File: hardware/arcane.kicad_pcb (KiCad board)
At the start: 2 copper layers, 24.8 x 28.5 mm, 7 parts, among them J1 Conn_01x02, J2 Conn_01x07, SW1 SW_Push, U1 XIAO-nRF52840-SMD

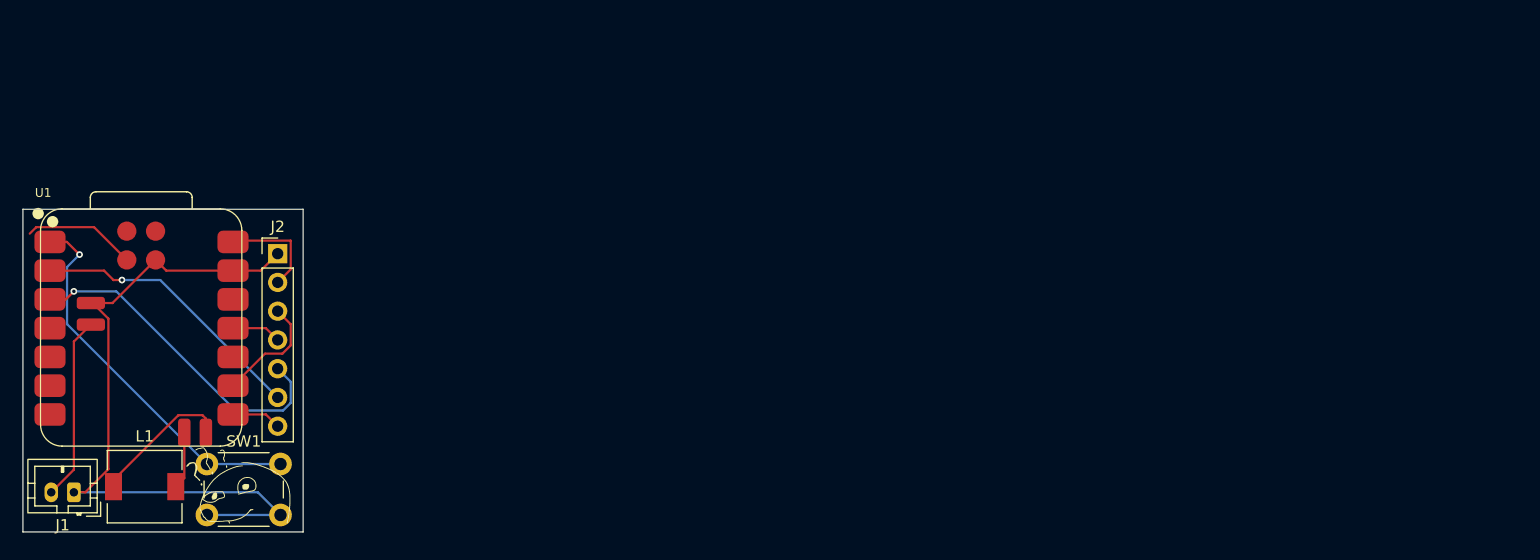
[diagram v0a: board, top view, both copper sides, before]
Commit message: migrate to stm32
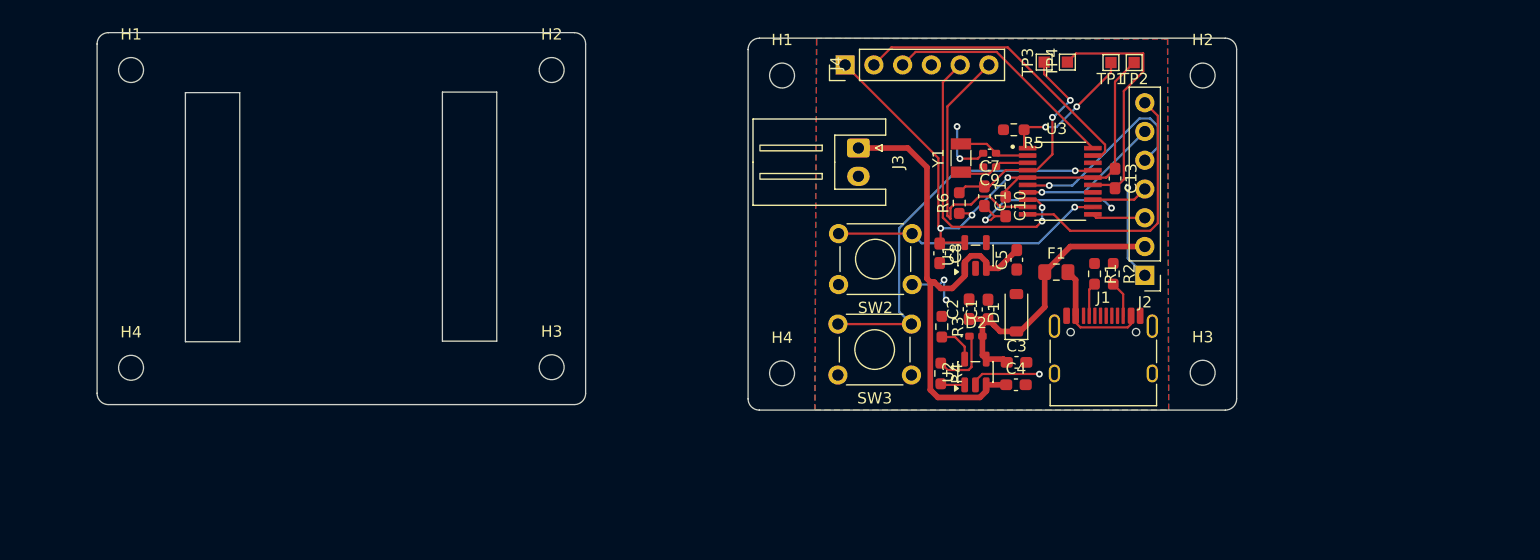
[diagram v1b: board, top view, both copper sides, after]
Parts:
- removed G*** (x2): LOGO, LOGO
- removed L1: L, Inductor_SMD:L_6.3x6.3_H3
- removed SW1: SW_Push, Button_Switch_THT:SW_PUSH_6mm
- added C1: 4.7uf, Capacitor_SMD:C_0603_1608Metric_Pad1.08x0.95mm_HandSolder, F.Cu at (161.5, 102.1)
- added C10: 100uf, Capacitor_SMD:C_0603_1608Metric_Pad1.08x0.95mm_HandSolder, F.Cu at (163.1, 93.0)
- added C11: 100nf, Capacitor_SMD:C_0603_1608Metric_Pad1.08x0.95mm_HandSolder, F.Cu at (161.2, 92.1)
- added C13: 100nf, Capacitor_SMD:C_0603_1608Metric_Pad1.08x0.95mm_HandSolder, F.Cu at (172.7, 90.5)
- added C2: 100nf, Capacitor_SMD:C_0603_1608Metric_Pad1.08x0.95mm_HandSolder, F.Cu at (159.8, 102.1)
- added C3: 4.7uf, Capacitor_SMD:C_0603_1608Metric_Pad1.08x0.95mm_HandSolder, F.Cu at (164.0, 106.8)
- added C4: 4.7uf, Capacitor_SMD:C_0603_1608Metric_Pad1.08x0.95mm_HandSolder, F.Cu at (164.0, 108.8)
- added C5: 10uf, Capacitor_SMD:C_0603_1608Metric_Pad1.08x0.95mm_HandSolder, F.Cu at (164.0, 97.7)
- added C7: 22pf, Capacitor_SMD:C_0402_1005Metric_Pad0.74x0.62mm_HandSolder, F.Cu at (161.6, 88.3)
- added C8: 10uf, Capacitor_SMD:C_0603_1608Metric_Pad1.08x0.95mm_HandSolder, F.Cu at (157.2, 97.1)
- added C9: 22pf, Capacitor_SMD:C_0402_1005Metric_Pad0.74x0.62mm_HandSolder, F.Cu at (161.6, 89.5)
- added D1: 5V, Diode_SMD:D_SOD-123, F.Cu at (164.0, 102.4)
- added D2: LED, LED_SMD:LED_0402_1005Metric_Pad0.77x0.64mm_HandSolder, F.Cu at (160.4, 104.5)
- added F1: Polyfuse, Fuse:Fuse_0805_2012Metric_Pad1.15x1.40mm_HandSolder, F.Cu at (167.5, 98.8)
- added H1: MountingHole, MountingHole:MountingHole_2.2mm_M2, F.Cu at (85.8, 81.0)
- added H1: MountingHole, MountingHole:MountingHole_2.2mm_M2, F.Cu at (143.3, 81.4)
- added H2: MountingHole, MountingHole:MountingHole_2.2mm_M2, F.Cu at (180.4, 81.4)
- added H2: MountingHole, MountingHole:MountingHole_2.2mm_M2, F.Cu at (123.0, 81.0)
- added H3: MountingHole, MountingHole:MountingHole_2.2mm_M2, F.Cu at (123.0, 107.2)
- added H3: MountingHole, MountingHole:MountingHole_2.2mm_M2, F.Cu at (180.4, 107.7)
- added H4: MountingHole, MountingHole:MountingHole_2.2mm_M2, F.Cu at (143.3, 107.7)
- added H4: MountingHole, MountingHole:MountingHole_2.2mm_M2, F.Cu at (85.8, 107.2)
- added J3: Conn_01x02, Connector_JST:JST_XH_S2B-XH-A_1x02_P2.50mm_Horizontal, F.Cu at (150.0, 87.8)
- added J4: Conn_01x06, Connector_PinHeader_2.54mm:PinHeader_1x06_P2.54mm_Vertical, F.Cu at (148.9, 80.5)
- added R1: 5.1K, Resistor_SMD:R_0603_1608Metric_Pad0.98x0.95mm_HandSolder, F.Cu at (170.9, 99.0)
- added R2: 5.1K, Resistor_SMD:R_0603_1608Metric_Pad0.98x0.95mm_HandSolder, F.Cu at (172.6, 99.0)
- added R3: 2K, Resistor_SMD:R_0603_1608Metric_Pad0.98x0.95mm_HandSolder, F.Cu at (157.4, 103.6)
- added R4: 470E, Resistor_SMD:R_0603_1608Metric_Pad0.98x0.95mm_HandSolder, F.Cu at (157.3, 107.8)
- added R5: 10K, Resistor_SMD:R_0603_1608Metric_Pad0.98x0.95mm_HandSolder, F.Cu at (163.8, 86.2)
- added R6: 10K, Resistor_SMD:R_0603_1608Metric_Pad0.98x0.95mm_HandSolder, F.Cu at (158.9, 92.7)
- added SW2: SW_Push, Button_Switch_THT:SW_TH_Tactile_Omron_B3F-100x, F.Cu at (154.8, 99.9)
- added SW3: SW_Push, Button_Switch_THT:SW_TH_Tactile_Omron_B3F-100x, F.Cu at (154.7, 107.9)
- added TP1: TestPoint, TestPoint:TestPoint_Pad_1.0x1.0mm, F.Cu at (172.3, 80.3)
- added TP2: TestPoint, TestPoint:TestPoint_Pad_1.0x1.0mm, F.Cu at (174.4, 80.3)
- added TP3: TestPoint, TestPoint:TestPoint_Pad_1.0x1.0mm, F.Cu at (166.4, 80.2)
- added TP4: TestPoint, TestPoint:TestPoint_Pad_1.0x1.0mm, F.Cu at (168.5, 80.2)
- added U2: MCP73831-2-OT, Package_TO_SOT_SMD:SOT-23-5, F.Cu at (160.4, 107.6)
- added U3: STM32L031F6P6, STM32:SOP65P640X120-20N, F.Cu at (167.9, 90.8)
- added Y1: Crystal, Crystal:Crystal_SMD_3215-2Pin_3.2x1.5mm, F.Cu at (159.1, 88.7)
- J1: value Conn_01x02 -> USB_C_Receptacle_USB2.0_16P; footprint Connector_JST:JST_PH_B2B-PH-K_1x02_P2.00mm_Vertical -> Connector_USB:USB_C_Receptacle_HRO_TYPE-C-31-M-12
- U1: value XIAO-nRF52840-SMD -> XC6220B331MR; footprint opl:XIAO-nRF52840-SMD -> Package_TO_SOT_SMD:SOT-23-5
- moved J1 91.7 mm to (171.7, 106.7), turned to 0 degrees
- moved J2 76.6 mm to (175.3, 99.1), turned to 180 degrees
- moved U1 73.9 mm to (160.4, 97.3), turned to 90 degrees
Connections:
- J2 pad 3: CLK -> /CLK
- J2 pad 4: DIN -> /DIN
- J2 pad 5: RST -> /RST
- J2 pad 6: DC -> /DC
- J2 pad 7: CS -> /CS
- U1 pad 1: Net-(U1-P0.02_A0_D0) -> /V_{BAT}
- U1 pad 2: DC -> GND
- U1 pad 3: RST -> /V_{BAT}
- U1 pad 4: BUSY -> unconnected-(U1-NC-Pad4)
- U1 pad 5: unconnected-(U1-P0.04_A4_D4_SDA-Pad5) -> +3.3V
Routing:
- net +3.3V: track 0.00 -> 53.2 mm, vias 0 -> 3
- net /V_{BAT}: track 0.00 -> 47.4 mm
- net Net-(U3-PA9): track 0.00 -> 34.6 mm, vias 0 -> 1
- net Net-(U1-P0.02_A0_D0): track 33.6 -> 0.00 mm, vias 1 -> 0
- net RST: track 29.7 -> 0.00 mm, vias 1 -> 0
- net /SWDIO: track 0.00 -> 26.5 mm
- net /UART TX: track 0.00 -> 26.3 mm, vias 0 -> 2
- net DC: track 24.7 -> 0.00 mm, vias 1 -> 0
- net Net-(U3-PA6): track 0.00 -> 24.1 mm, vias 0 -> 1
- net /UART RX: track 0.00 -> 23.8 mm
- net /CS: track 0.00 -> 23.5 mm
- net /SWCLK: track 0.00 -> 20.8 mm
- net Net-(U3-NRST): track 0.00 -> 19.4 mm, vias 0 -> 2
- net /RST: track 0.00 -> 17.7 mm, vias 0 -> 1
- net VBUS: track 9.31 -> 25.9 mm
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- added copper zone on B.Cu, net GND
- added copper zone on F.Cu, net GND
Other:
- board size 24.8 x 28.5 mm -> 100.6 x 33.3 mm
- board text removed: "ARCANE"

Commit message: update: zine, firmware and gerber
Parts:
- SW2, SW3: footprint Button_Switch_THT:SW_TH_Tactile_Omron_B3F-100x -> Button_Switch_SMD:SW_SPST_TL3342
- moved C11 25.6 mm to (185.9, 98.6)
- moved C2 25.6 mm to (184.6, 108.6)
- moved C3 25.6 mm to (188.8, 113.3)
- moved C5 25.6 mm to (188.8, 104.2)
- moved C7 25.6 mm to (186.4, 94.8)
- moved C8 25.6 mm to (182.0, 103.7)
- moved C9 25.6 mm to (186.4, 96.0)
- moved D1 25.6 mm to (188.8, 108.9)
- moved H2 25.6 mm to (205.2, 88.0)
- moved H3 25.6 mm to (205.2, 114.2)
- moved J2 25.6 mm to (200.1, 105.6)
- moved R3 25.6 mm to (182.2, 110.1)
- moved R4 25.6 mm to (182.1, 114.3)
- moved R6 25.6 mm to (183.7, 99.2)
- moved TP1 25.6 mm to (197.1, 86.8)
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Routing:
- net Net-(U3-PA6): track 24.1 -> 36.1 mm, vias 1 -> 2
- net Net-(U3-PA9): track 34.6 -> 38.4 mm, vias 1 -> 2
- net GND: track 61.3 -> 61.4 mm, vias 8 -> 21
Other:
- board size 100.6 x 33.3 mm -> 110.2 x 33.1 mm
